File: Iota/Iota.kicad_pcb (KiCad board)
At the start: 2 copper layers, 26.6 x 43.5 mm, 19 parts, among them J1 USB_B_Mini, J2 Conn_01x12_Male, J3 Conn_01x12_Male, J4 Conn_01x05_Male, SW1 SW_DIP_x01, U1 ATmega32U4-AU, Y1 16MHz

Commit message: Cleaned up and submitted to Seeed
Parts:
- added C15: 0.1uF, Capacitors_SMD:C_0805, F.Cu at (141.9, 86.2)
- added G1: LOGO, Iota:hanko, F.Cu at (133.5, 81.7)
- moved J4 2.23 mm to (138.8, 100.9)
- moved R1 0.11 mm to (141.2, 88.0)
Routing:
- net GND: track 26.1 -> 36.7 mm, vias 18 -> 21
- net D4: track 18.6 -> 16.5 mm
- net RESET: track 29.8 -> 27.9 mm
- net D5: track 20.9 -> 19.7 mm
- net Vcc: track 92.6 -> 92.1 mm
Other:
- board size 26.6 x 43.5 mm -> 28.7 x 42.3 mm
- board text removed: "AC3DN"

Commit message: Minor changes
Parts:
- J1: footprint Connectors:USB_Micro-B -> Connectors:USB_Mini-B
- moved C6 4.54 mm to (141.4, 70.2), turned to 270 degrees
- moved R7 1.73 mm to (135.3, 70.9)
- moved R5 1.73 mm to (132.9, 70.9)
- moved J1 0.25 mm to (133.5, 64.8), turned to 270 degrees
- moved J4 0.14 mm to (138.8, 100.8)
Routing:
- net GND: track 36.7 -> 47.3 mm
- net Vcc: track 92.1 -> 83.7 mm
- net D-: track 6.34 -> 4.57 mm
- net D+: track 6.98 -> 5.39 mm
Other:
- board size 28.7 x 42.3 mm -> 27.7 x 43.4 mm
- board text added: "Ɩota 1.1 AC3DN"
- board text removed: "Ɩota 1.0"

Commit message: Added power LED
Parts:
- added LED2: green, LEDs:LED_Rectangular_W3.9mm_H1.8mm, F.Cu at (141.5, 63.2)
- added R3: 1K0, Resistors_SMD:R_0805, F.Cu at (145.2, 64.1)
- C2, C4: value 10pF -> 22pF
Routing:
- net Vcc: track 83.7 -> 90.8 mm
- net Net-(LED2-Pad1): track 0.00 -> 3.62 mm
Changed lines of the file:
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@@
-(kicad_pcb (version 20171130) (host pcbnew "(5.0.1-3-g963ef8bb5)")
+(kicad_pcb (version 20171130) (host pcbnew "(5.1.0-0)")
   (general
     (thickness 1.6)
     (drawings 36)
-    (tracks 270)
+    (tracks 274)
     (zones 0)
-    (modules 21)
-    (nets 40)
+    (modules 23)
+    (nets 41)
   )
   (page A4)
@@
   )
   (setup
-    (last_trace_width 0.25)
+    (last_trace_width 0.5)
     (user_trace_width 0.5)
     (trace_clearance 0.2)
@@
     (zone_45_only no)
     (trace_min 0.2)
-    (segment_width 0.2)
-    (edge_width 0.15)
     (via_size 0.8)
     (via_drill 0.4)
@@
     (uvia_min_size 0.2)
     (uvia_min_drill 0.1)
+    (edge_width 0.15)
+    (segment_width 0.2)
     (pcb_text_width 0.3)
     (pcb_text_size 1.5 1.5)
@@
   (net 38 "Net-(LED1-Pad1)")
   (net 39 "Net-(R1-Pad2)")
+  (net 40 "Net-(LED2-Pad1)")
   (net_class Default "This is the default net class."
     (clearance 0.2)
@@
     (add_net "Net-(J1-Pad4)")
     (add_net "Net-(LED1-Pad1)")
+    (add_net "Net-(LED2-Pad1)")
     (add_net "Net-(R1-Pad2)")
     (add_net RESET)
@@
       (effects (font (size 1 1) (thickness 0.15)))
     )
-    (fp_text value 10pF (at 0 1.75 90) (layer F.Fab)
+    (fp_text value 22pF (at 0 1.75 90) (layer F.Fab)
       (effects (font (size 1 1) (thickness 0.15)))
     )
@@
       (effects (font (size 1 1) (thickness 0.15)))
     )
-    (fp_text value 10pF (at 0 1.75 90) (layer F.Fab)
+    (fp_text value 22pF (at 0 1.75 90) (layer F.Fab)
       (effects (font (size 1 1) (thickness 0.15)))
     )
@@
     (tags "USB USB_B USB_Mini connector")
     (attr smd)
-    (fp_text reference J1 (at -0.9652 -6.6548) (layer F.SilkS)
+    (fp_text reference J1 (at -3.91668 -6.604) (layer F.SilkS)
       (effects (font (size 1 1) (thickness 0.15)))
     )
@@
     (pad 1 smd rect (at 2.8 -1.6 270) (size 2.3 0.5) (layers F.Cu F.Paste F.Mask)
       (net 18 Vcc))
+  )
+  (module LEDs:LED_Rectangular_W3.9mm_H1.8mm (layer F.Cu)
+    (at 141.54404 63.16472 270)
+    (descr "LED_Rectangular, Rectangular,  Rectangular size 3.9x1.8mm^2, 2 pins, http://www.kingbright.com/attachments/file/psearch/000/00/00/L-2774GD(Ver.7B).pdf")
+    (tags "LED_Rectangular Rectangular  Rectangular size 3.9x1.8mm^2 2 pins")
+    (fp_text reference LED2 (at 1.33096 -1.89992 270) (layer F.SilkS)
+      (effects (font (size 1 1) (thickness 0.15)))
+    )
+    (fp_text value green (at 1.27 1.935 270) (layer F.Fab)
+      (effects (font (size 1 1) (thickness 0.15)))
+    )
+    (fp_line (start 3.7 -1.2) (end -1.15 -1.2) (layer F.CrtYd) (width 0.05))
+    (fp_line (start 3.7 1.2) (end 3.7 -1.2) (layer F.CrtYd) (width 0.05))
+    (fp_line (start -1.15 1.2) (end 3.7 1.2) (layer F.CrtYd) (width 0.05))
+    (fp_line (start -1.15 -1.2) (end -1.15 1.2) (layer F.CrtYd) (width 0.05))
+    (fp_line (start 3.28 0.825) (end 3.28 0.935) (layer F.SilkS) (width 0.12))
+    (fp_line (start 3.28 -0.935) (end 3.28 -0.825) (layer F.SilkS) (width 0.12))
+    (fp_line (start 3.27 0.935) (end 3.28 0.935) (layer F.SilkS) (width 0.12))
+    (fp_line (start 1.08 0.935) (end 1.811 0.935) (layer F.SilkS) (width 0.12))
+    (fp_line (start 3.27 -0.935) (end 3.28 -0.935) (layer F.SilkS) (width 0.12))
+    (fp_line (start 1.08 -0.935) (end 1.811 -0.935) (layer F.SilkS) (width 0.12))
+    (fp_line (start 3.22 -0.875) (end -0.68 -0.875) (layer F.Fab) (width 0.1))
+    (fp_line (start 3.22 0.875) (end 3.22 -0.875) (layer F.Fab) (width 0.1))
+    (fp_line (start -0.68 0.875) (end 3.22 0.875) (layer F.Fab) (width 0.1))
+    (fp_line (start -0.68 -0.875) (end -0.68 0.875) (layer F.Fab) (width 0.1))
+    (pad 2 thru_hole circle (at 2.54 0 270) (size 1.8 1.8) (drill 0.9) (layers *.Cu *.Mask)
+      (net 18 Vcc))
+    (pad 1 thru_hole rect (at 0 0 270) (size 1.8 1.8) (drill 0.9) (layers *.Cu *.Mask)
+      (net 40 "Net-(LED2-Pad1)"))
+    (model ${KISYS3DMOD}/LEDs.3dshapes/LED_Rectangular_W3.9mm_H1.8mm.wrl
+      (at (xyz 0 0 0))
+      (scale (xyz 0.393701 0.393701 0.393701))
+      (rotate (xyz 0 0 0))
+    )
+  )
+  (module Resistors_SMD:R_0805 (layer F.Cu)
+    (at 145.161 64.12484 270)
+    (descr "Resistor SMD 0805, reflow soldering, Vishay (see dcrcw.pdf)")
+    (tags "resistor 0805")
+    (attr smd)
+    (fp_text reference R3 (at 0 -1.65 270) (layer F.SilkS)
+      (effects (font (size 1 1) (thickness 0.15)))
+    )
+    (fp_text value 1K0 (at 0 1.75 270) (layer F.Fab)
+      (effects (font (size 1 1) (thickness 0.15)))
+    )
+    (fp_line (start 1.55 0.9) (end -1.55 0.9) (layer F.CrtYd) (width 0.05))
+    (fp_line (start 1.55 0.9) (end 1.55 -0.9) (layer F.CrtYd) (width 0.05))
+    (fp_line (start -1.55 -0.9) (end -1.55 0.9) (layer F.CrtYd) (width 0.05))
+    (fp_line (start -1.55 -0.9) (end 1.55 -0.9) (layer F.CrtYd) (width 0.05))
+    (fp_line (start -0.6 -0.88) (end 0.6 -0.88) (layer F.SilkS) (width 0.12))
+    (fp_line (start 0.6 0.88) (end -0.6 0.88) (layer F.SilkS) (width 0.12))
+    (fp_line (start -1 -0.62) (end 1 -0.62) (layer F.Fab) (width 0.1))
+    (fp_line (start 1 -0.62) (end 1 0.62) (layer F.Fab) (width 0.1))
+    (fp_line (start 1 0.62) (end -1 0.62) (layer F.Fab) (width 0.1))
+    (fp_line (start -1 0.62) (end -1 -0.62) (layer F.Fab) (width 0.1))
+    (fp_text user %R (at 0 0 270) (layer F.Fab)
+      (effects (font (size 0.5 0.5) (thickness 0.075)))
+    )
+    (pad 2 smd rect (at 0.95 0 270) (size 0.7 1.3) (layers F.Cu F.Paste F.Mask)
+      (net 1 GND))
+    (pad 1 smd rect (at -0.95 0 270) (size 0.7 1.3) (layers F.Cu F.Paste F.Mask)
+      (net 40 "Net-(LED2-Pad1)"))
+    (model ${KISYS3DMOD}/Resistors_SMD.3dshapes/R_0805.wrl
+      (at (xyz 0 0 0))
+      (scale (xyz 1 1 1))
+      (rotate (xyz 0 0 0))
+    )
   )
   (gr_circle (center 139.4968 76.2254) (end 140.1318 76.2) (layer F.SilkS) (width 0.2))
@@
   (segment (start 127.764499 97.398799) (end 131.1402 100.7745) (width 0.25) (layer F.Cu) (net 18))
   (segment (start 127.764499 91.8972) (end 127.764499 97.398799) (width 0.25) (layer F.Cu) (net 18))
+  (segment (start 145.034 69.19468) (end 145.034 71.374) (width 0.5) (layer F.Cu) (net 18))
+  (segment (start 141.54404 65.70472) (end 145.034 69.19468) (width 0.5) (layer F.Cu) (net 18))
   (via (at 137.033 85.979) (size 0.8) (drill 0.4) (layers F.Cu B.Cu) (net 19))
   (segment (start 136.9945 86.0175) (end 137.033 85.979) (width 0.25) (layer F.Cu) (net 19))
@@
   (segment (start 139.7256 87.488) (end 140.2232 87.9856) (width 0.25) (layer F.Cu) (net 39))
   (segment (start 137.7945 87.488) (end 139.7256 87.488) (width 0.25) (layer F.Cu) (net 39))
+  (segment (start 145.15088 63.16472) (end 145.161 63.17484) (width 0.5) (layer F.Cu) (net 40))
+  (segment (start 141.54404 63.16472) (end 145.15088 63.16472) (width 0.5) (layer F.Cu) (net 40))
   (zone (net 1) (net_name GND) (layer F.Cu) (hatch edge 0.508)
     (connect_pads (clearance 0.508))

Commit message: Bumped version to 1.2
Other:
- board text added: "Ɩota 1.2 AC3DN"
- board text removed: "Ɩota 1.1 AC3DN"
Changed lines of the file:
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@@
   )
   (setup
-    (last_trace_width 0.5)
+    (last_trace_width 0.25)
     (user_trace_width 0.5)
     (trace_clearance 0.2)
@@
   (gr_line (start 147.4597 59.7916) (end 147.4724 103.1875) (layer Edge.Cuts) (width 0.15))
   (gr_line (start 119.761 59.8) (end 147.4978 59.8) (layer Edge.Cuts) (width 0.15))
-  (gr_text "Ɩota\n1.1\nAC3DN" (at 124.0282 64.4398) (layer B.SilkS)
+  (gr_text "Ɩota\n1.2\nAC3DN" (at 124.0282 64.4398) (layer B.SilkS)
     (effects (font (size 1.5 1.5) (thickness 0.3)) (justify mirror))
   )
-  (gr_text "Ɩota\n1.1\nAC3DN" (at 124.1806 64.4398) (layer F.SilkS)
+  (gr_text "Ɩota\n1.2\nAC3DN" (at 124.1806 64.4398) (layer F.SilkS)
     (effects (font (size 1.5 1.5) (thickness 0.3)))
   )

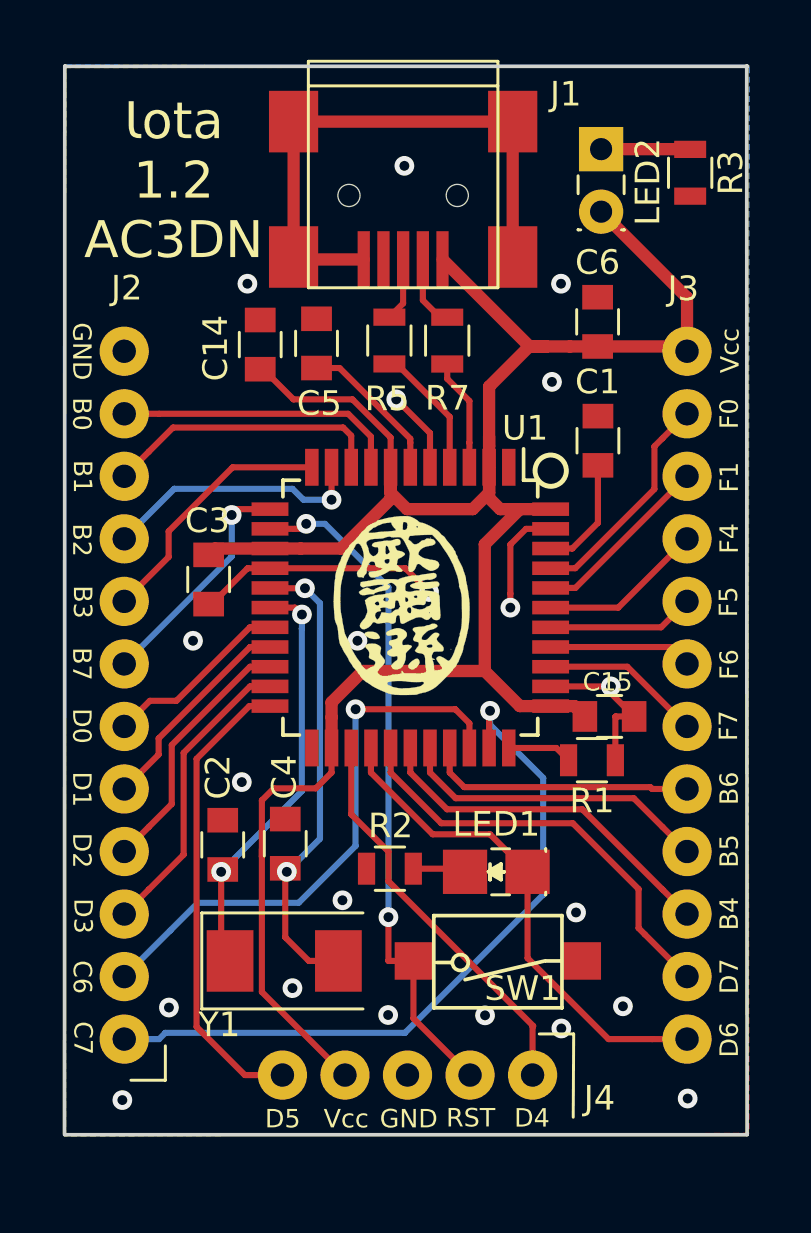
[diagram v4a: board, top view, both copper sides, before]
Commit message: Update to QFN44 chip
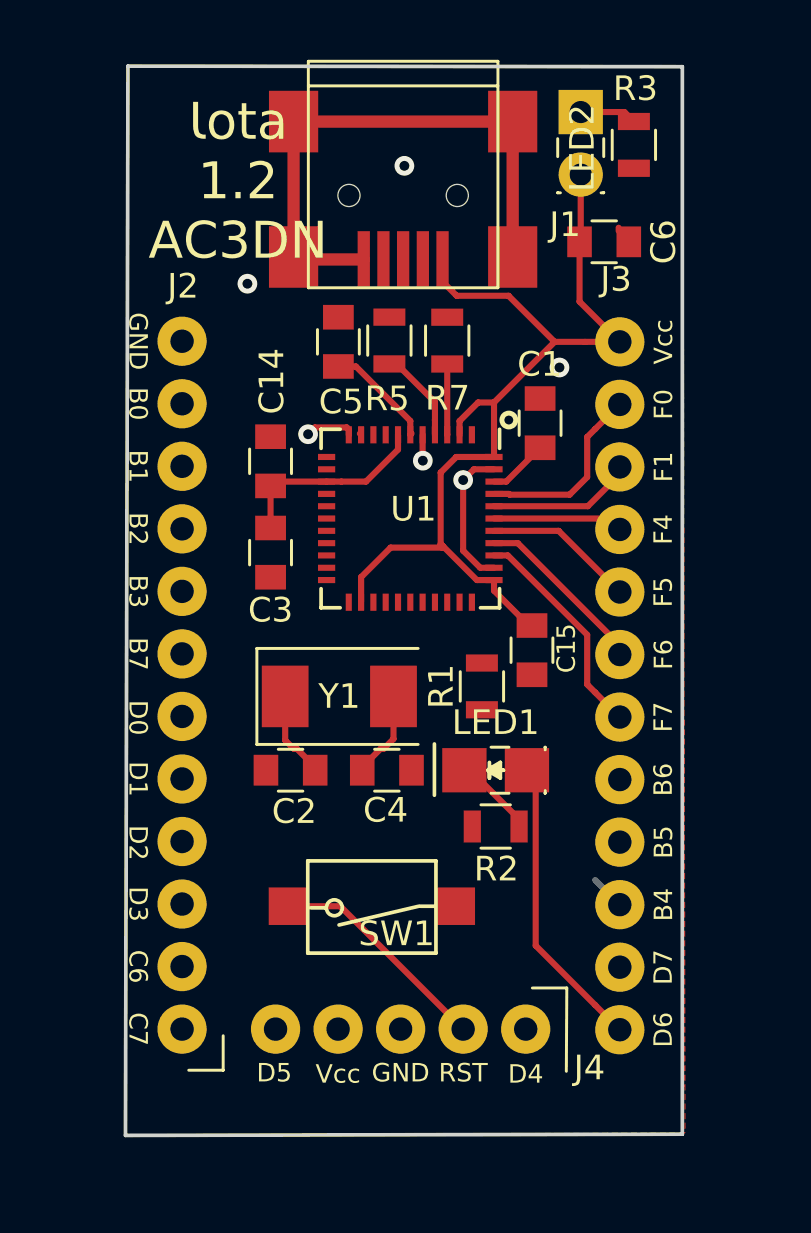
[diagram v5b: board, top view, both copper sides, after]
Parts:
- G1: moved to B.Cu
- U1: value ATmega32U4-AU -> ATmega32U4-MU; footprint Housings_QFP:TQFP-44_10x10mm_Pitch0.8mm -> Iota:QFN-44-1EP_7x7mm_Pitch0.5mm
- moved G1 18.4 mm to (140.5, 64.7)
- moved Y1 11.0 mm to (130.9, 85.4)
- moved SW1 5.58 mm to (132.2, 94.0)
- moved R1 5.38 mm to (136.7, 85.0), turned to 90 degrees
- moved C4 5.09 mm to (132.8, 88.4), turned to 0 degrees
- moved C14 4.76 mm to (128.1, 75.8)
- moved R2 4.62 mm to (137.3, 90.7)
- moved C15 4.14 mm to (138.7, 83.5), turned to 90 degrees
- moved LED1 4.13 mm to (136.0, 88.4)
- moved C2 4.10 mm to (128.9, 88.4), turned to 180 degrees
- moved U1 3.62 mm to (133.8, 78.2)
- moved C6 3.26 mm to (141.7, 66.9), turned to 180 degrees
- moved J3 2.76 mm to (142.3, 71.0)
- moved C3 2.74 mm to (128.1, 79.6)
- moved R3 2.55 mm to (142.9, 63.0)
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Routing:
- net Vcc: track 90.8 -> 48.2 mm
- net C7: track 29.3 -> 0.00 mm, vias 1 -> 0
- net C6: track 23.0 -> 0.00 mm, vias 1 -> 0
- net D5: track 19.6 -> 0.00 mm
- net RESET: track 27.7 -> 9.20 mm, vias 2 -> 0
- net GND: track 47.3 -> 29.8 mm, vias 21 -> 5
- net D7: track 17.4 -> 0.00 mm
- net D4: track 16.4 -> 0.00 mm
- net Net-(C4-Pad1): track 19.1 -> 3.60 mm, vias 2 -> 0
- net Net-(C2-Pad1): track 17.0 -> 3.58 mm, vias 2 -> 0
- net B4: track 14.6 -> 1.41 mm
- net B5: track 12.8 -> 0.00 mm
- net D3: track 12.2 -> 0.00 mm
- net B0: track 11.7 -> 0.00 mm
- net B1: track 11.5 -> 0.00 mm
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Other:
- board size 27.7 x 43.4 mm -> 22.6 x 43.4 mm

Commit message: Board layout is clean
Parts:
- moved R2 30.9 mm to (126.1, 61.9), turned to 90 degrees
- moved G1 29.5 mm to (134.2, 93.5)
- moved LED1 25.6 mm to (126.1, 64.8), turned to 270 degrees
- moved R1 2.58 mm to (138.9, 86.4)
- moved C15 1.22 mm to (138.8, 82.3)
- moved C2 1.11 mm to (128.6, 89.5)
- moved C4 1.11 mm to (132.5, 89.5)
- moved Y1 1.11 mm to (130.6, 86.5)
- moved C14 0.46 mm to (127.7, 75.8)
- moved C3 0.46 mm to (127.7, 79.6)
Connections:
- LED1 pad 2: D6 -> B0
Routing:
- net RESET: track 9.20 -> 46.5 mm, vias 0 -> 2
- net Vcc: track 48.2 -> 76.6 mm, vias 0 -> 2
- net C7: track 0.00 -> 25.7 mm, vias 0 -> 1
- net C6: track 0.00 -> 23.6 mm, vias 0 -> 1
- net D5: track 0.00 -> 21.2 mm
- net D4: track 0.00 -> 19.9 mm
- net GND: track 29.8 -> 49.3 mm, vias 5 -> 16
- net D7: track 0.00 -> 19.0 mm
- net D3: track 0.00 -> 16.8 mm, vias 0 -> 1
- net B0: track 0.00 -> 16.5 mm
- net B4: track 1.41 -> 17.3 mm
- net B5: track 0.00 -> 15.7 mm
- net D2: track 0.00 -> 15.1 mm, vias 0 -> 1
- net D1: track 0.00 -> 13.5 mm, vias 0 -> 1
- net B6: track 0.00 -> 13.0 mm
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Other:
- board size 22.6 x 43.4 mm -> 22.6 x 41.7 mm

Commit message: Ready for PCB fabrication
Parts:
- LED1, LED2: footprint LEDs:LED_Rectangular_W3.9mm_H1.8mm -> LEDs:LED_1206
- moved LED2 4.58 mm to (140.7, 66.2)
- moved R3 2.48 mm to (140.7, 61.9), turned to 90 degrees
- moved C6 1.54 mm to (142.8, 65.9), turned to 270 degrees
- moved LED1 1.47 mm to (126.1, 66.3)
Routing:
- net Vcc: track 76.6 -> 75.9 mm
- net B0: track 16.5 -> 15.9 mm
- net Net-(LED2-Pad1): track 2.32 -> 1.77 mm
- net GND: track 49.3 -> 49.4 mm, vias 16 -> 17
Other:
- board size 22.6 x 41.7 mm -> 22.9 x 42.6 mm

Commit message: Final for 1.2
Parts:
- added F1: 500mA, Fuse_Holders_and_Fuses:Fuse_SMD1206_Wave, F.Cu at (137.7, 70.4)
- moved R5 1.43 mm to (131.5, 70.8)
- moved R7 1.43 mm to (133.9, 70.8)
- moved C5 1.43 mm to (129.5, 70.9)
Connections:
- J1 pad 1: Vcc -> Net-(F1-Pad2)
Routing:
- net GND: track 49.4 -> 77.8 mm, vias 17 -> 18
- net Vcc: track 75.9 -> 69.2 mm
- net Net-(F1-Pad2): track 0.00 -> 3.98 mm
- net Net-(C5-Pad2): track 4.49 -> 5.96 mm
- net B5: track 15.7 -> 14.4 mm
- net B4: track 17.3 -> 16.2 mm
- net Net-(J1-Pad3): track 2.57 -> 3.73 mm
- net D+: track 4.07 -> 4.84 mm
- net D-: track 2.88 -> 3.57 mm
